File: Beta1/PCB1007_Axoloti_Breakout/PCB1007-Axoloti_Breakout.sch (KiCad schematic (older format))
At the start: 22 parts, among them J1 Axoloti_40Pin, J2 FPC_20POS

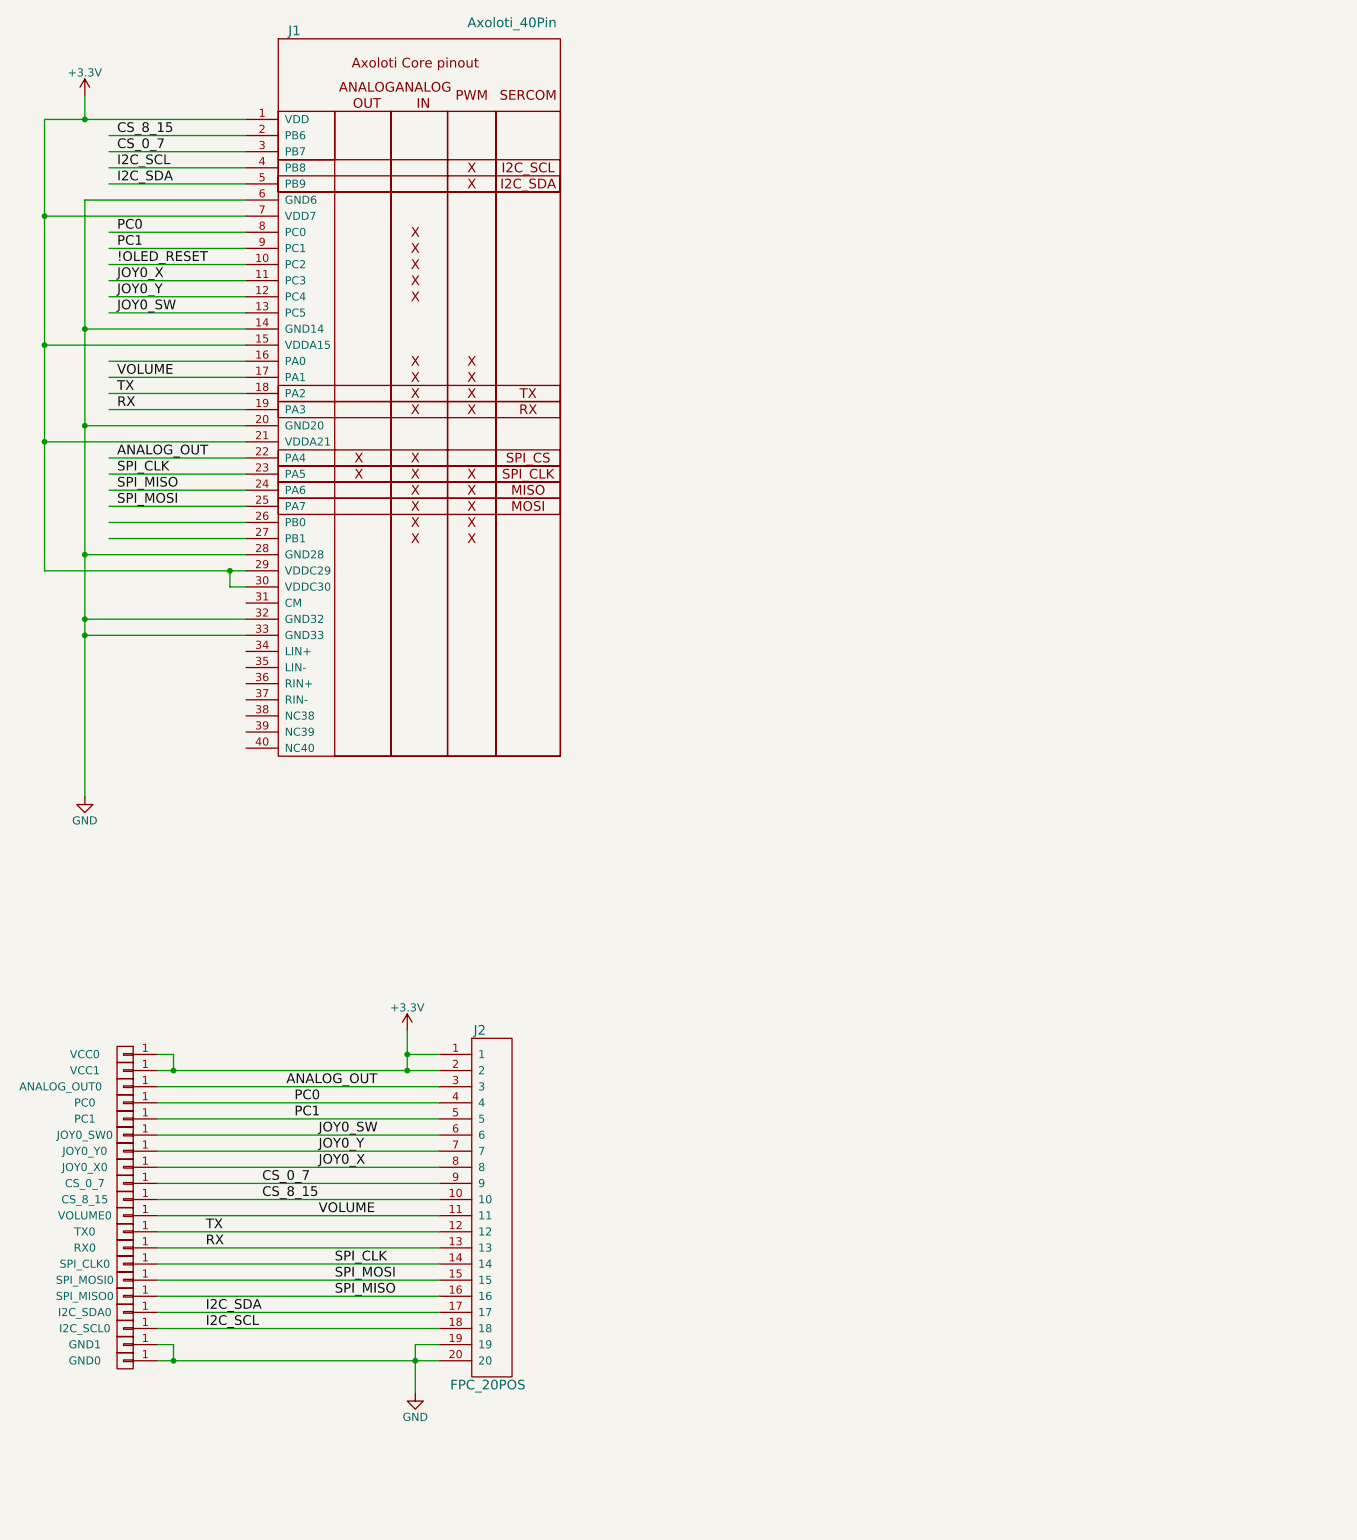
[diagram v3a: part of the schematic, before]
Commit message: Changed con pinout. Ready for Fab.
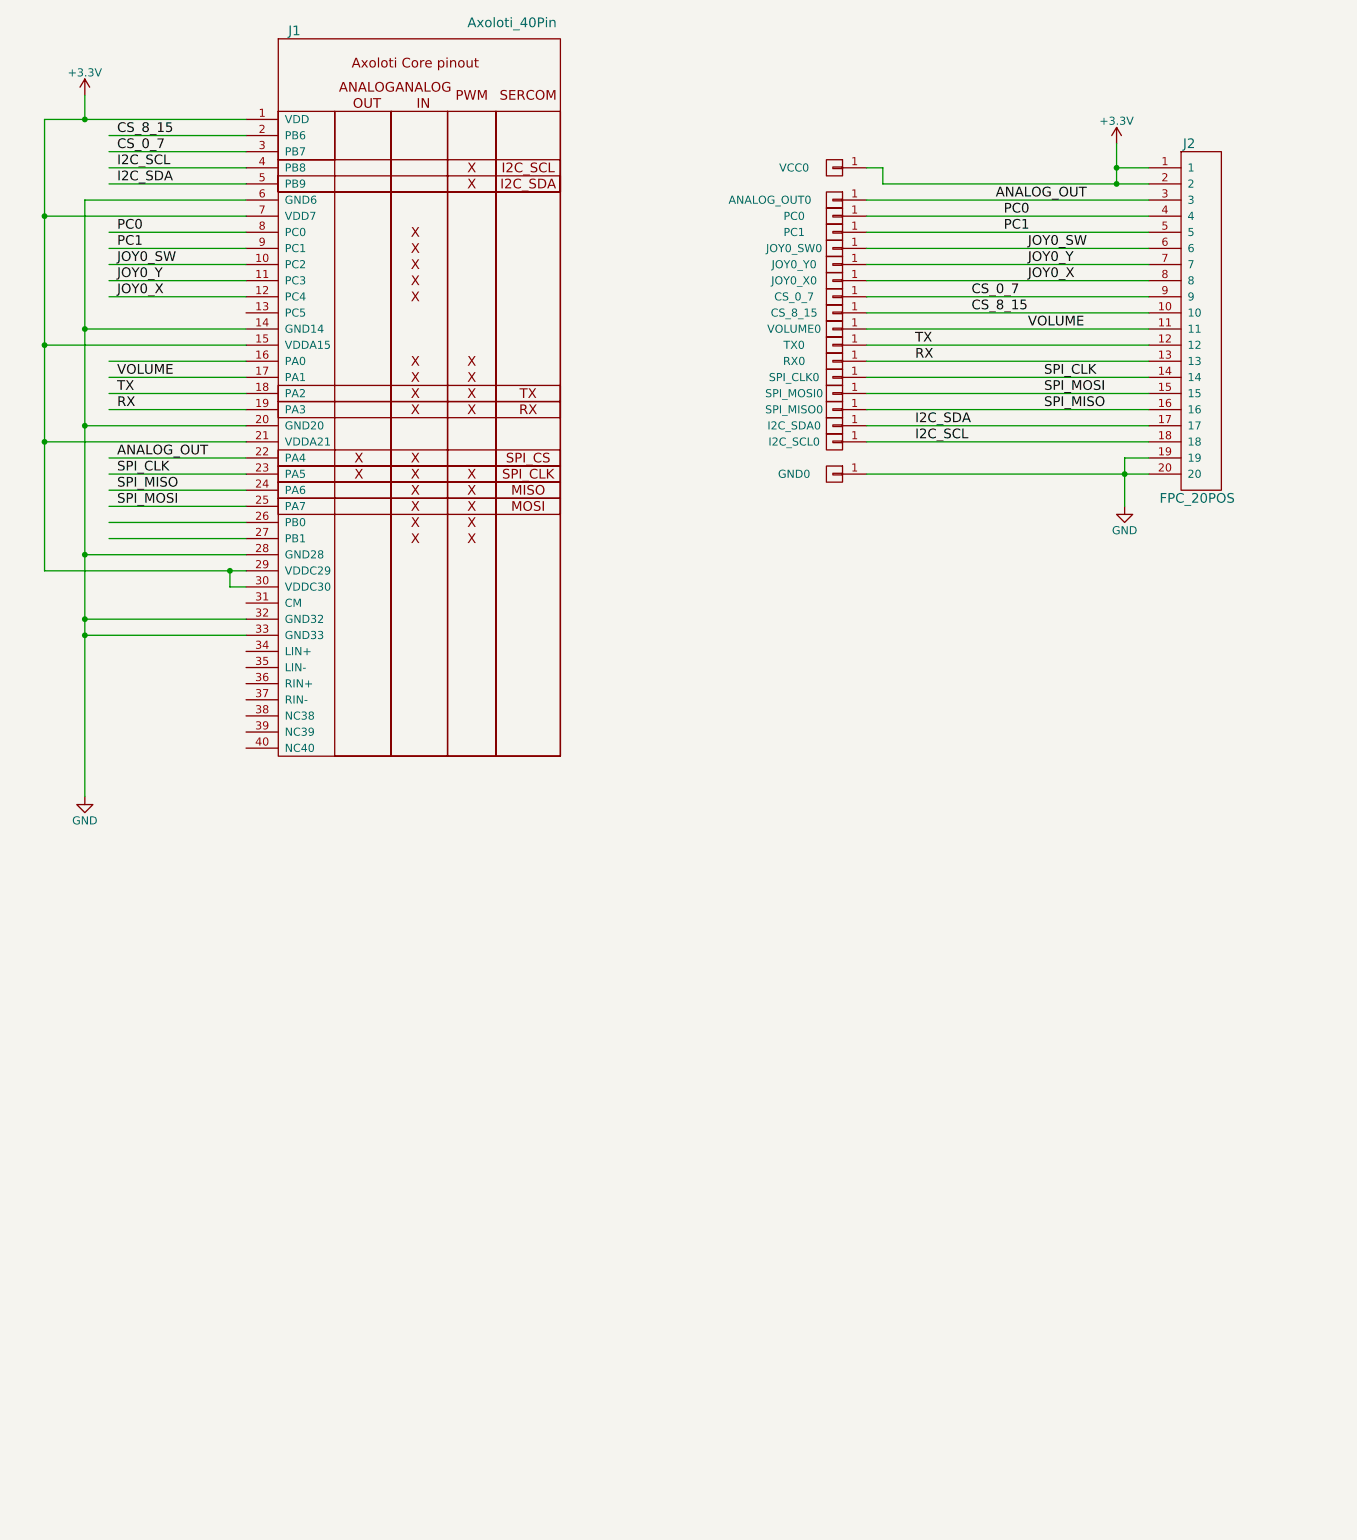
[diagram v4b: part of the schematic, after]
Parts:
- removed GND1, VCC1: CONN_01X01, Liberry:single_0.1, symbol CONN_01X01
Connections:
- net labels removed: !OLED_RESET
- wire segments 62 -> 59
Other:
- moved on the sheet: ANALOG_OUT0, CS_0_7, CS_8_15, GND0, I2C_SCL0, I2C_SDA0, J2, JOY0_SW0, JOY0_X0, JOY0_Y0, PC0, PC1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
